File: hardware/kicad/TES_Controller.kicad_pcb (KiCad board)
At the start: 2 copper layers, 64.1 x 89.3 mm, 81 parts

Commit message: Use one resistor value for the whole divider upper arm
Chris pointed out the upper arm could be three 115k rather than
118k + 115k + 115k. He is right, and my reason for the mixed values had
already expired: I picked them to sum to exactly 348k so the firmware
coefficient would not move, but moving the ADS1115 to 3.3 V changes R11 and
therefore the coefficient regardless. There was nothing left to preserve.

Every figure is effectively unchanged — 39.0 V per resistor against the same
1.9x margin, 4.869 vs 4.910 mV per LSB, a 140.2 V ceiling instead of 141.4 V
— and it drops a part number. That is not only the parts: JLCPCB charges a
setup fee per distinct component in SMT assembly.

Coefficient becomes 38.954, (345k + 9.09k) / 9.09k.

Also in this commit, recovering from something that has now happened twice:
KiCad was open on an old copy of the project the whole time we were working,
and on closing it wrote that copy back. The schematic lost all 8 components
added since (R33, R34, D9, D10, W1-W4) and the project file regained the
HV120 and Power netclasses along with a 0.2 mm clearance, which is where 534
DRC violations appeared from — against netclasses deleted days earlier. The
.kicad_dru was untouched, since KiCad does not rewrite it.

tools/check_project.py compares the settings that matter and regen_hw.sh
runs it before DRC, so the next occurrence is a one-line message rather than
a debugging session. The two .lck files were committed by accident and are
now untracked and ignored.

Co-Authored-By: Claude Opus 5 <noreply@anthropic.com>
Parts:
- R10: value RT0603BRD07118KL -> RT0603BRD07115KL

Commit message: Update the board signature for V1.3
"TES SECC V1.2 | Chris Huang | 2025" becomes "TES SECC V1.3 | Chris Huang &
Claude | 2026", at Chris's request.

The longer string needs 28.69 mm rather than 22.70 mm, and the old anchor
would have pushed it up into W4's wire pad. Moving the anchor down to
y = 148.60 uses the space below instead — CN3 only reaches x ≈ 180.5, so
the strip at x > 181 is clear all the way to the bottom edge. It now sits
0.51 mm from the right edge, 0.84 mm from the bottom, and 1.9 mm clear of
W4, with no silkscreen warnings of its own.

English rather than Chinese: KiCad's stroke font has no CJK coverage, and a
TrueType fallback at 0.89 mm would not be legible on silkscreen anyway —
Chinese characters need roughly twice that height to survive the process.

Also removed one dangling via left behind by the divider rework.

Co-Authored-By: Claude Opus 5 <noreply@anthropic.com>
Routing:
- net 5V: vias 7 -> 6
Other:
- board text added: "TES SECC V1.3 | Chris Huang & Claude | 2026"
- board text removed: "TES SECC V1.2 | Chris Huang | 2025"

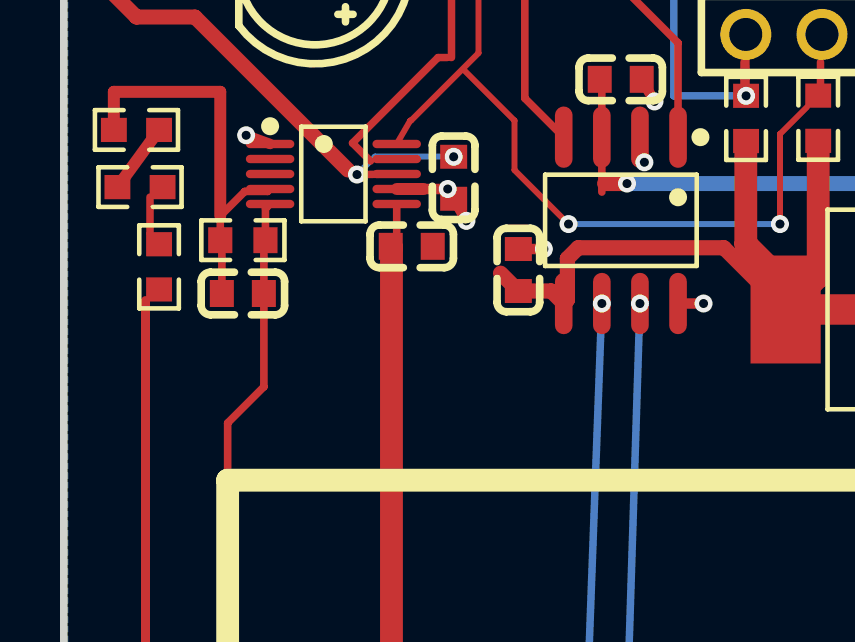
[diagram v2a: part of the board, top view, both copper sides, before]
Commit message: Identify the board revision with a divider on ADS1115 AIN3
The U13 EEPROM could not be placed: SDA, SCL and VCC all had to reach it,
and the nearest free spot was 32 mm from the I2C pins. AIN3 was tied to
ground and only served as the CP measurement's negative input, so it now
carries HW_ID from R36/R37 (10k/10k = level 6 = V1.3). Old boards read
0 V and keep the 30.000 coefficient; one net reaches U5 instead of three.

Schematic 236/236 zero difference, ERC 0. PCB hand-routed on the top
layer, DRC 0 errors / 0 unconnected, warnings unchanged at 182,
mechanical lock untouched. R35 and D10 are still to be applied.

Co-Authored-By: Claude Opus 5.5 <noreply@anthropic.com>
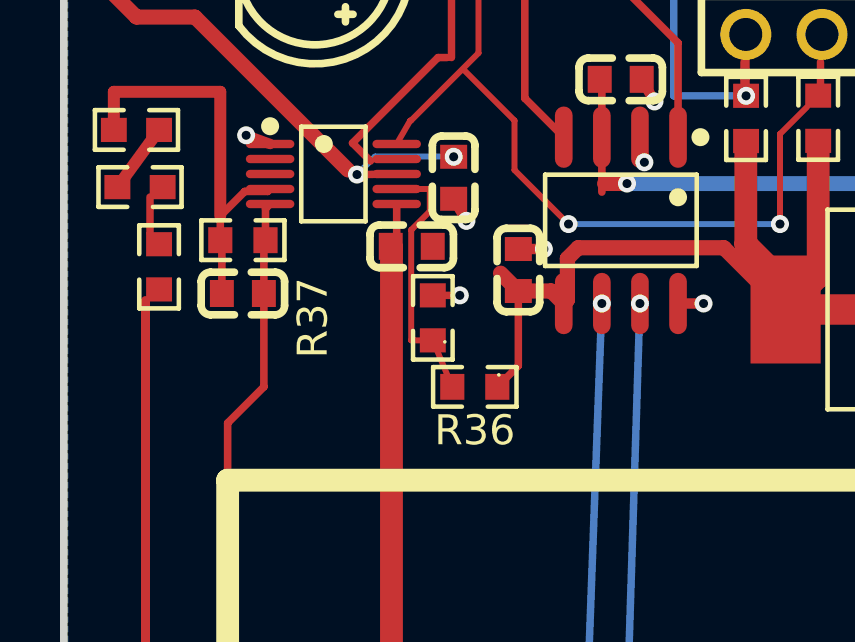
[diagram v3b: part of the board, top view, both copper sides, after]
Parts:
- added R36: 0603WAF1002T5E, R0603, F.Cu at (133.7, 94.1)
- added R37: 0603WAF1002T5E, R0603, F.Cu at (132.3, 91.8)
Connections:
- U5 pad 7: GND -> HW_ID
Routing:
- net HW_ID: track 0.00 -> 8.81 mm
- net VDD33: track 133.5 -> 137.0 mm
- net GND: track 56.1 -> 55.3 mm

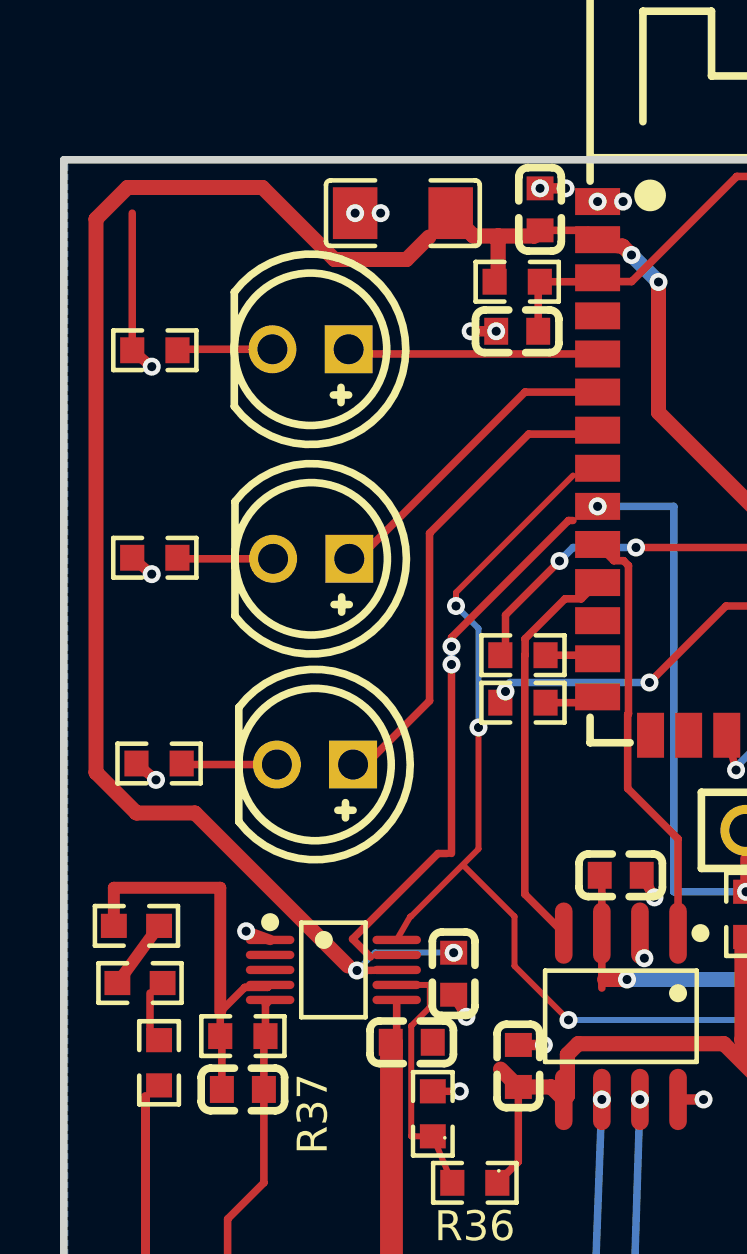
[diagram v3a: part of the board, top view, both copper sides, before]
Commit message: Feed the ADS1115's VDD33 from the C28 side instead of the board edge
Moving the ADS1115 back to 3.3 V left U5.8 on a 31 mm trace down the left
edge from C1, past the HV divider, with C20 reached only through a bottom
detour and a via in its pad. A dangling VDD33 stub at C28 already pointed
at U5. Connect U5.8 straight to C20 and the stub to C20 on the top layer,
and remove the edge trace, the detour and two vias (VDD33 137 -> 97 mm).

DRC 0 errors / 0 unconnected, warnings unchanged at 182, mechanical lock
untouched. The grid router's layer and via costs are why it happened;
recorded in CLAUDE.md.

Co-Authored-By: Claude Opus 5.5 <noreply@anthropic.com>
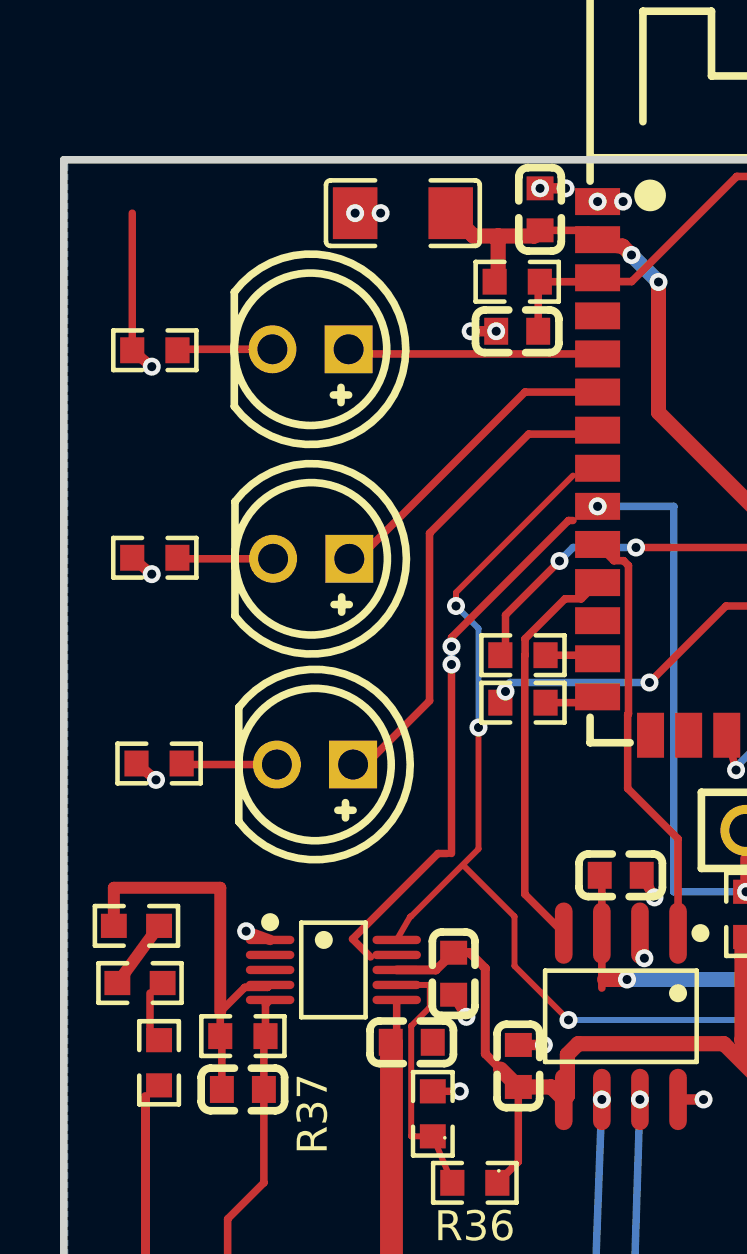
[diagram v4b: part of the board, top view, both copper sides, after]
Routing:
- net VDD33: track 137.0 -> 97.1 mm, vias 9 -> 7

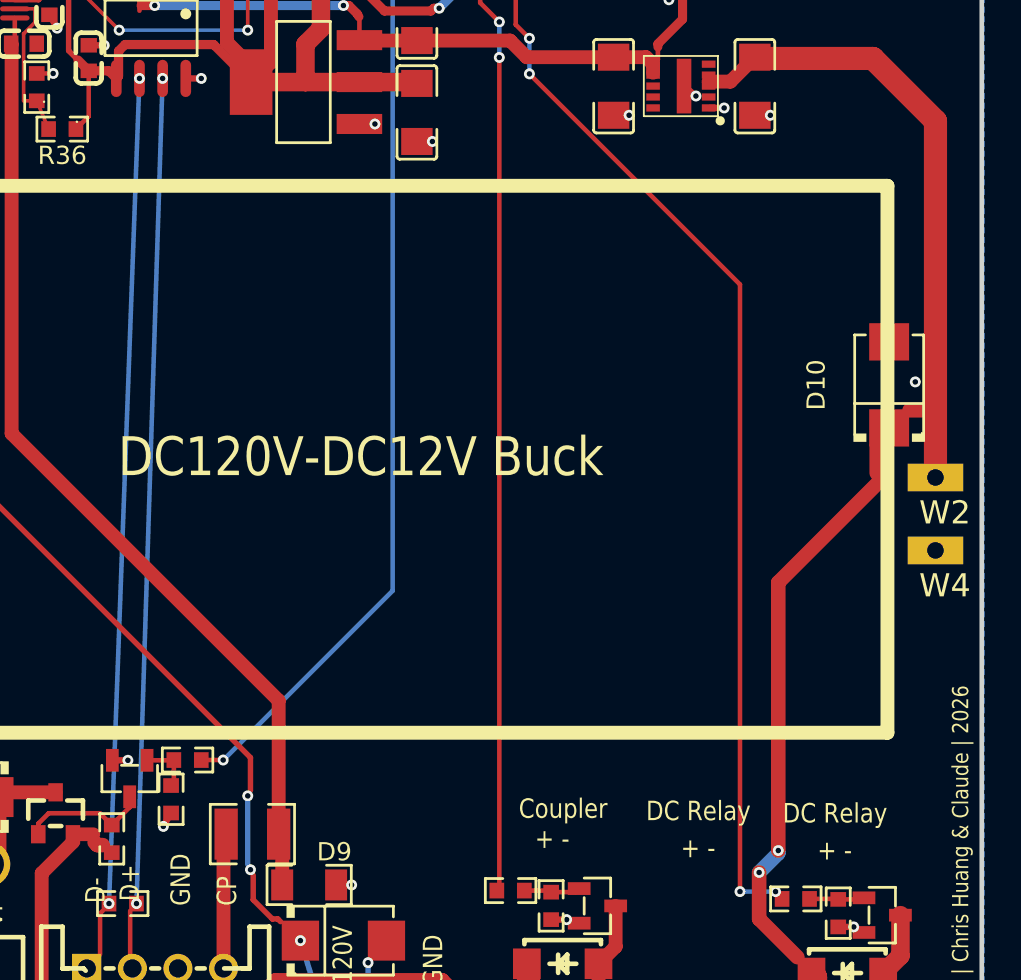
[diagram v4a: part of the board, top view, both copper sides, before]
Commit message: Put R35 and D10 on the board: the PCB now matches the schematic
R35 (Q4 gate divider) sits in the gap east of R26 under Q2, top layer
only. D10 (SMBJ12A) moves out from under the buck module to directly
north of W2, its 12V pad on the trunk; the trunk jogs around its ground
pad, which drops to two plane vias. The 12V branch into the board used
to reach W2 only by touching D10's old pad; it now goes straight to W2.

Both hand-placed after the auto-placer put D10 16.6 mm from W2. Netlist
236/236 zero difference, DRC 0 errors / 0 unconnected, warnings 182 ->
181, mechanical lock untouched.

Co-Authored-By: Claude Opus 5.5 <noreply@anthropic.com>
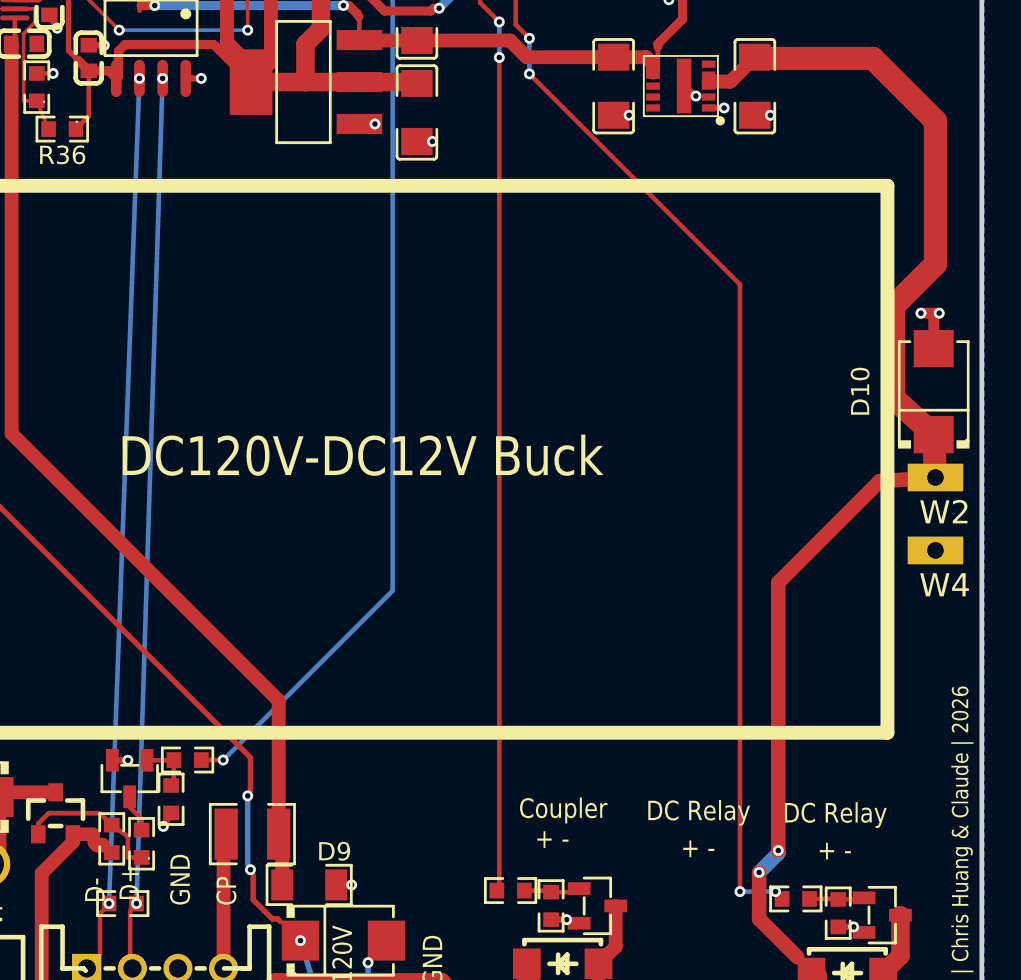
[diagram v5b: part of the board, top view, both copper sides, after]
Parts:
- added R35: 0603WAF1002T5E, R0603, F.Cu at (138.1, 133.3)
- D10: value SMBJ13A -> SMBJ12A
- moved D10 2.47 mm to (181.5, 108.5)
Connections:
- Q2 pad 3: VP_PGATE -> VP_PGATE_DRV
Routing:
- net GND: track 55.3 -> 58.3 mm, vias 63 -> 64
- net 12V: track 131.1 -> 133.8 mm
- net VP_PGATE_DRV: track 0.00 -> 2.10 mm
- net VP_PGATE: track 7.08 -> 8.10 mm

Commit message: Put the Turtle Power logo on both silkscreen layers
9 mm on top, in the only free spot north of the buck module, and 20 mm
on the bottom, clear of the bottom-layer traces. tools/make_logo.py
turns the line-drawing PNG into board-only silkscreen footprints; the
drawing's strokes are 0.066 mm at 9 mm, below JLCPCB's silkscreen
minimum, so it dilates them to about 0.23 mm.

DRC 0 errors / 0 unconnected, warnings unchanged at 181, netlist still
236/236, mechanical lock untouched.

Co-Authored-By: Claude Opus 5.5 <noreply@anthropic.com>
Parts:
- added LOGO1: LOGO_TurtlePower_9mm, LOGO_TurtlePower_9mm, F.Cu at (177.6, 91.9)
- added LOGO2: LOGO_TurtlePower_20mm, LOGO_TurtlePower_20mm, B.Cu at (164.5, 113.0)

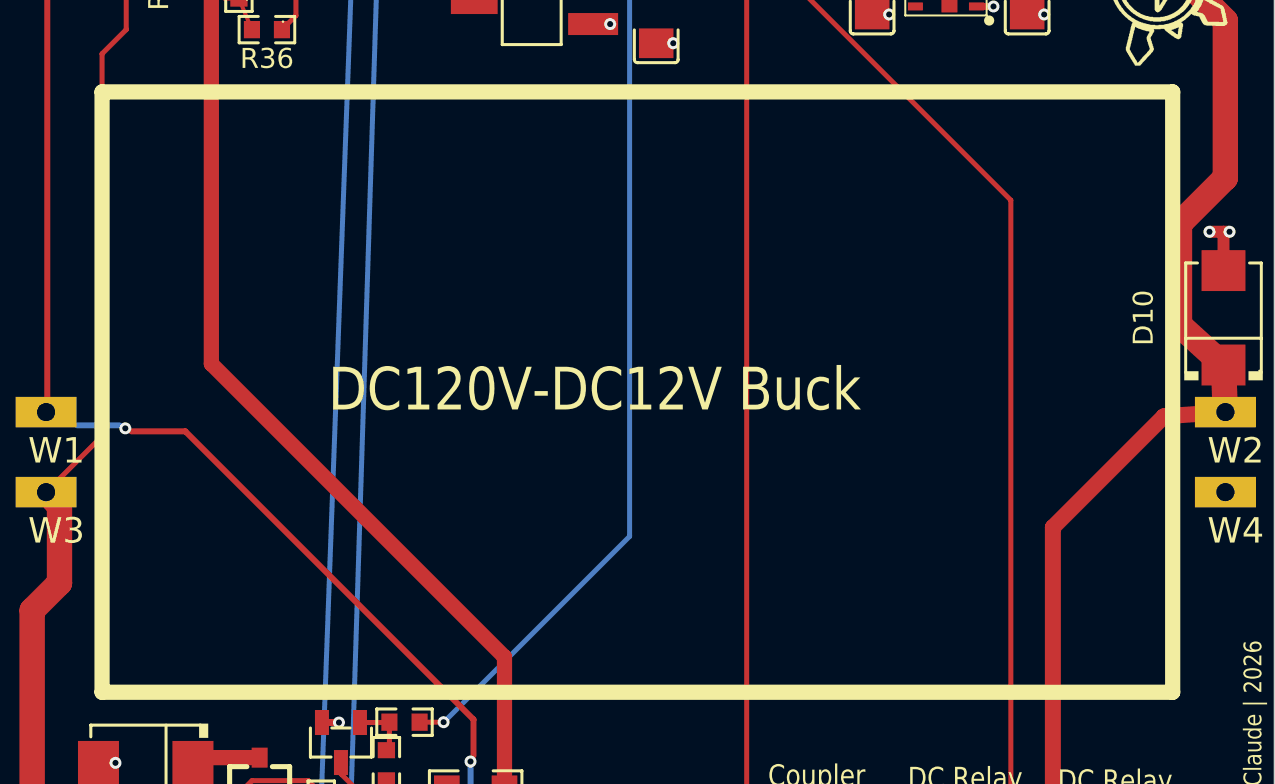
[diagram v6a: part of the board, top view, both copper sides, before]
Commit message: Restore the mounting holes and generate the V1.3 fabrication files
The four Ø3.2 holes under the buck module - its nylon standoffs and the
enclosure's fixing points - were drawn in EasyEDA as filled circles on the
Multi-Layer and never made it into the KiCad board. The mechanical lock
stayed green because it reads the EasyEDA export. They are back as NPTH
with a small copper keepout, and tools/check_mech_kicad.py now checks the
holes and locked positions against the KiCad board itself.

tools/make_fab.sh writes Gerbers and drills with JLCPCB's settings and a
JLCPCB BOM/CPL built from bom.csv plus changes_v13.py: 69 SMT parts in 31
line items, 15 hand-soldered. The 115k 0.1% divider resistors use
RT0603BRE07115KL because the specified BRD part was nearly out of stock.

DRC 0 errors / 0 unconnected, netlist 236/236, mechanical check passes.

Co-Authored-By: Claude Opus 5.5 <noreply@anthropic.com>
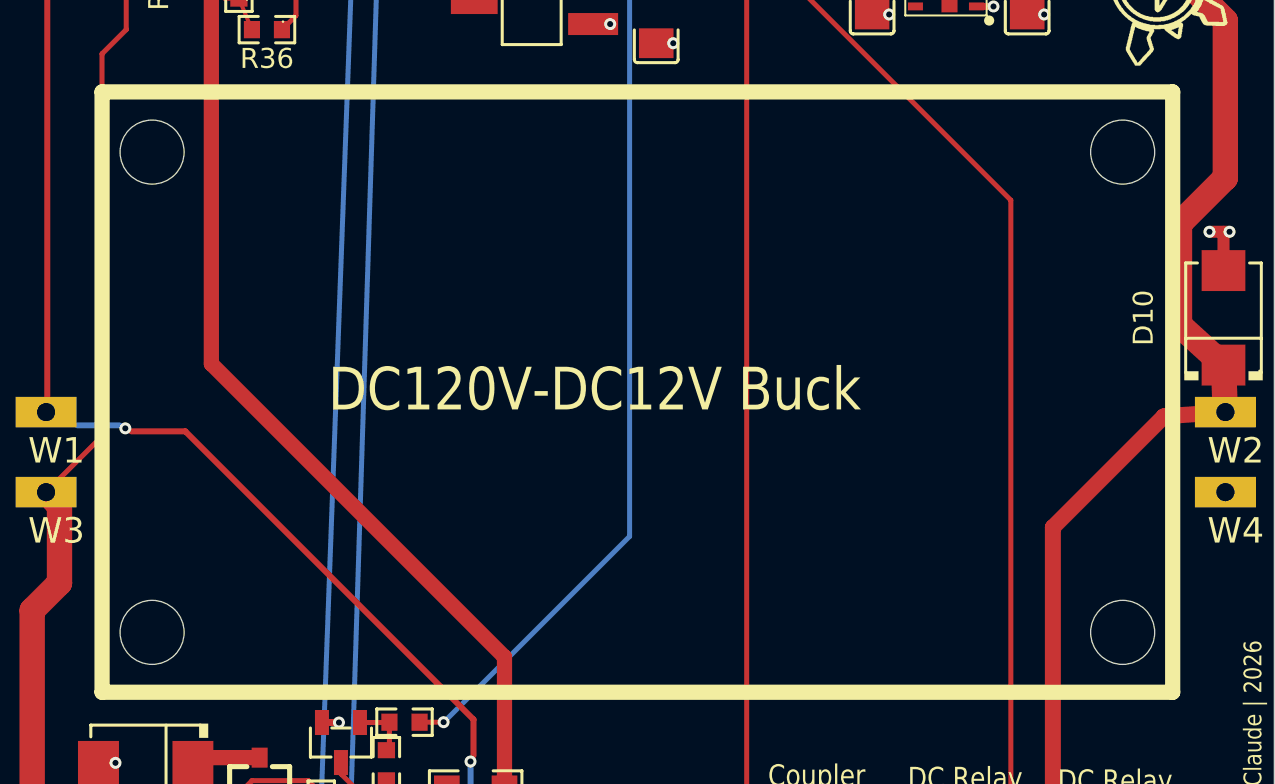
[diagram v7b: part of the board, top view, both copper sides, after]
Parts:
- added MH1: MountingHole_3.2mm_NPTH_Keepout4.6mm, MountingHole_3.2mm_NPTH_Keepout4.6mm, F.Cu at (128.0, 100.2)
- added MH2: MountingHole_3.2mm_NPTH_Keepout4.6mm, MountingHole_3.2mm_NPTH_Keepout4.6mm, F.Cu at (176.5, 100.2)
- added MH3: MountingHole_3.2mm_NPTH_Keepout4.6mm, MountingHole_3.2mm_NPTH_Keepout4.6mm, F.Cu at (128.0, 124.2)
- added MH4: MountingHole_3.2mm_NPTH_Keepout4.6mm, MountingHole_3.2mm_NPTH_Keepout4.6mm, F.Cu at (176.5, 124.2)

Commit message: Use RT0603BRE07115KL for the 115k divider resistors throughout
The specified RT0603BRD07115KL was down to 2 in stock and the board needs
3. The user accepted the same Yageo RT thin-film part with TCR code E, so
the schematic, the board and the JLCPCB BOM now all carry it instead of
the BOM alone substituting it. JLCPCB's order number is left for their
engineers to place.

Schematic 236/236, ERC 0, DRC 0 errors / 0 unconnected, mechanical check
passes. The regenerated Gerbers differ from the last ones only in date
stamps and aperture-select ordering.

Co-Authored-By: Claude Opus 5.5 <noreply@anthropic.com>
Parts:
- R10: value RT0603BRD07115KL -> RT0603BRE07115KL
- R33, R34: value 115k -> RT0603BRE07115KL
